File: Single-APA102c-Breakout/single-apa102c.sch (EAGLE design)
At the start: 4 parts

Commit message: moved led to a 45 degree angle
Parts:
- added U$2: CMD_C0DE_LOGOCMD_CODE_LOGO_TOP_COPPER, logos:CMD_C0DE_LOGOCMD_CODE_LOGO_TOP_COPPER
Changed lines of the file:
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@@
 <part name="J1" library="connector" deviceset="M04" device="PTH"/>
 <part name="J2" library="connector" deviceset="M02" device="PTH"/>
+<part name="U$2" library="logos" deviceset="CMD_C0DE_LOGO" device="CMD_CODE_LOGO_TOP_COPPER"/>
 </parts>
 <sheets>
@@
 </nets>
 </sheet>
+<sheet>
+<plain>
+</plain>
+<instances>
+<instance part="U$2" gate="G$1" x="38.1" y="53.34" smashed="yes"/>
+</instances>
+<busses>
+</busses>
+<nets>
+</nets>
+</sheet>

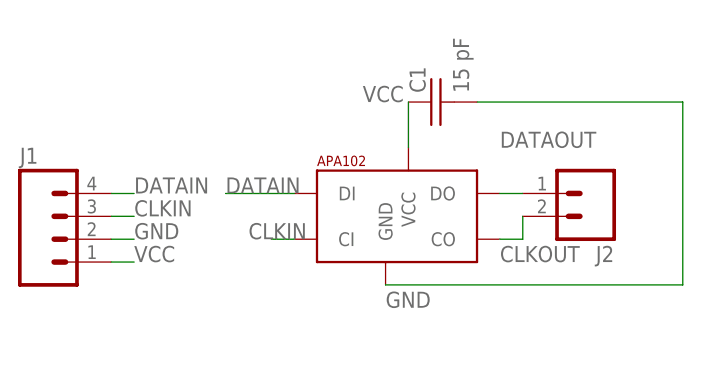
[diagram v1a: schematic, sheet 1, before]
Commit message: adding outputs to right side
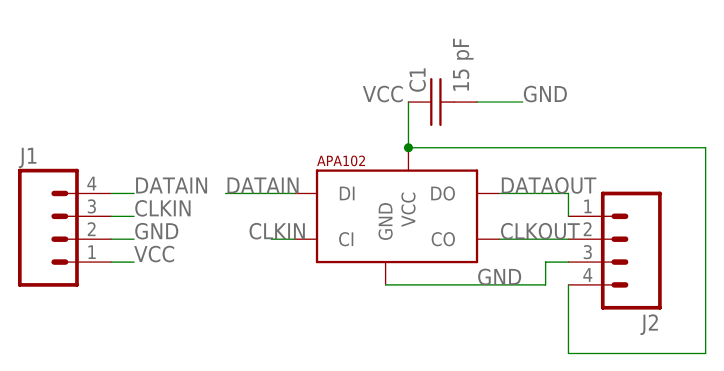
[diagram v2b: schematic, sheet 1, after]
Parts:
- J2: device connector:M02PTH -> connector:M04PTH
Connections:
- net GND: now also J2.3
- net VCC: now also J2.4
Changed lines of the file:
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@@
 <part name="C1" library="passives" deviceset="C-US" device="C0805K" package3d_urn="urn:adsk.eagle:package:8089589/1" value="15 pF"/>
 <part name="J1" library="connector" deviceset="M04" device="PTH"/>
-<part name="J2" library="connector" deviceset="M02" device="PTH"/>
 <part name="U$2" library="logos" deviceset="CMD_C0DE_LOGO" device="CMD_CODE_LOGO_TOP_COPPER"/>
+<part name="J2" library="connector" deviceset="M04" device="PTH"/>
 </parts>
 <sheets>
@@
 <attribute name="NAME" x="-2.54" y="51.562" size="1.778" layer="95"/>
 </instance>
-<instance part="J2" gate="G$1" x="60.96" y="48.26" smashed="yes" rot="R180">
-<attribute name="VALUE" x="63.5" y="53.34" size="1.778" layer="96" rot="R180"/>
-<attribute name="NAME" x="63.5" y="42.418" size="1.778" layer="95" rot="R180"/>
+<instance part="J2" gate="G$1" x="63.5" y="43.18" smashed="yes" rot="R180">
+<attribute name="VALUE" x="68.58" y="50.8" size="1.778" layer="96" rot="R180"/>
+<attribute name="NAME" x="68.58" y="34.798" size="1.778" layer="95" rot="R180"/>
 </instance>
 </instances>
@@
 <pinref part="C1" gate="G$1" pin="1"/>
 <label x="35.56" y="58.42" size="1.778" layer="95"/>
+<wire x1="40.64" y1="53.34" x2="73.66" y2="53.34" width="0.1524" layer="91"/>
+<wire x1="73.66" y1="53.34" x2="73.66" y2="30.48" width="0.1524" layer="91"/>
+<junction x="40.64" y="53.34"/>
+<wire x1="73.66" y1="30.48" x2="58.42" y2="30.48" width="0.1524" layer="91"/>
+<pinref part="J2" gate="G$1" pin="4"/>
+<wire x1="58.42" y1="30.48" x2="58.42" y2="38.1" width="0.1524" layer="91"/>
 </segment>
 <segment>
@@
 <net name="GND" class="0">
 <segment>
-<pinref part="U$1" gate="G$1" pin="GND"/>
-<pinref part="C1" gate="G$1" pin="2"/>
-<wire x1="48.26" y1="58.42" x2="71.12" y2="58.42" width="0.1524" layer="91"/>
-<wire x1="71.12" y1="58.42" x2="71.12" y2="38.1" width="0.1524" layer="91"/>
-<wire x1="71.12" y1="38.1" x2="38.1" y2="38.1" width="0.1524" layer="91"/>
-<label x="38.1" y="35.56" size="1.778" layer="95"/>
-</segment>
-<segment>
 <pinref part="J1" gate="G$1" pin="2"/>
 <wire x1="7.62" y1="43.18" x2="10.16" y2="43.18" width="0.1524" layer="91"/>
 <label x="10.16" y="43.18" size="1.778" layer="95"/>
 </segment>
-</net>
-<net name="DATAOUT" class="0">
 <segment>
-<pinref part="U$1" gate="G$1" pin="DO"/>
-<pinref part="J2" gate="G$1" pin="1"/>
-<wire x1="50.8" y1="48.26" x2="53.34" y2="48.26" width="0.1524" layer="91"/>
-<label x="50.8" y="53.34" size="1.778" layer="95"/>
+<pinref part="C1" gate="G$1" pin="2"/>
+<wire x1="48.26" y1="58.42" x2="53.34" y2="58.42" width="0.1524" layer="91"/>
+<label x="53.34" y="58.42" size="1.778" layer="95"/>
 </segment>
-</net>
-<net name="CLKOUT" class="0">
 <segment>
-<pinref part="U$1" gate="G$1" pin="CO"/>
-<wire x1="50.8" y1="43.18" x2="53.34" y2="43.18" width="0.1524" layer="91"/>
-<pinref part="J2" gate="G$1" pin="2"/>
-<wire x1="53.34" y1="43.18" x2="53.34" y2="45.72" width="0.1524" layer="91"/>
-<label x="50.8" y="40.64" size="1.778" layer="95"/>
+<pinref part="U$1" gate="G$1" pin="GND"/>
+<wire x1="38.1" y1="38.1" x2="55.88" y2="38.1" width="0.1524" layer="91"/>
+<wire x1="55.88" y1="38.1" x2="55.88" y2="40.64" width="0.1524" layer="91"/>
+<pinref part="J2" gate="G$1" pin="3"/>
+<wire x1="55.88" y1="40.64" x2="58.42" y2="40.64" width="0.1524" layer="91"/>
+<label x="48.26" y="38.1" size="1.778" layer="95"/>
 </segment>
 </net>
@@
 </segment>
 </net>
+<net name="DATAOUT" class="0">
+<segment>
+<pinref part="U$1" gate="G$1" pin="DO"/>
+<wire x1="50.8" y1="48.26" x2="58.42" y2="48.26" width="0.1524" layer="91"/>
+<pinref part="J2" gate="G$1" pin="1"/>
+<wire x1="58.42" y1="48.26" x2="58.42" y2="45.72" width="0.1524" layer="91"/>
+<label x="50.8" y="48.26" size="1.778" layer="95"/>
+</segment>
+</net>
+<net name="CLKOUT" class="0">
+<segment>
+<pinref part="U$1" gate="G$1" pin="CO"/>
+<pinref part="J2" gate="G$1" pin="2"/>
+<wire x1="50.8" y1="43.18" x2="58.42" y2="43.18" width="0.1524" layer="91"/>
+<label x="50.8" y="43.18" size="1.778" layer="95"/>
+</segment>
+</net>
